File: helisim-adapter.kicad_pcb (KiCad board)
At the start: 2 copper layers, 68.6 x 30.5 mm, 5 parts, among them J1 NUCLEO_CN7, J2 NUCLEO_CN10, J3 TIVA_J1_J3, J4 TIVA_J4_J2, J5 HeliConn

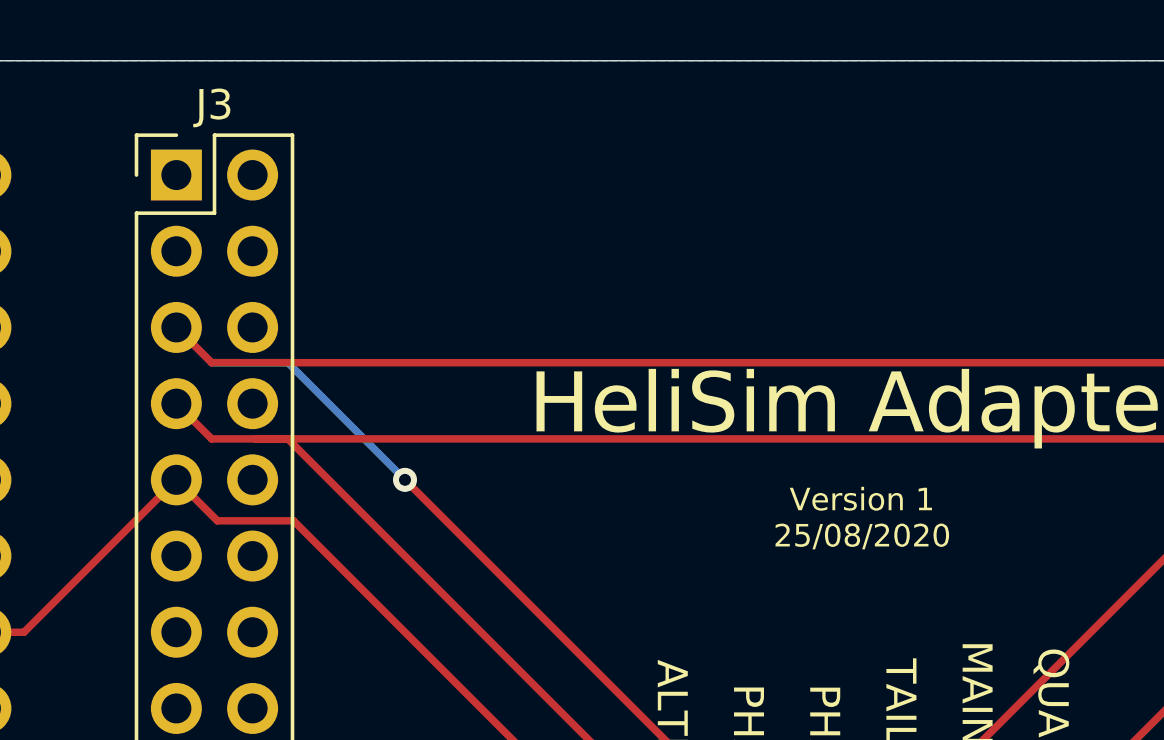
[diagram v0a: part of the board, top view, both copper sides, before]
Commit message: Fixed silkscreen designator for tiva jumper
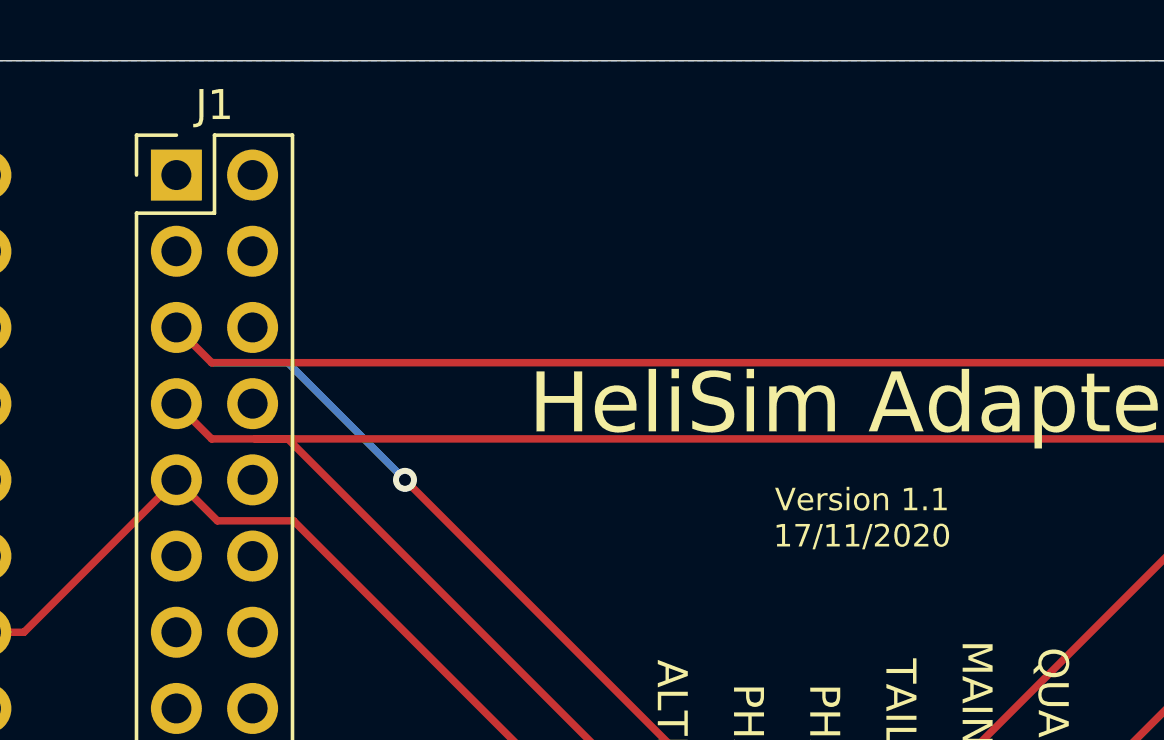
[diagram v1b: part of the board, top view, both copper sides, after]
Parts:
- renumbered J3 to J1
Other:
- board text added: "Version 1.1 17/11/2020"
- board text removed: "Version 1 25/08/2020"
